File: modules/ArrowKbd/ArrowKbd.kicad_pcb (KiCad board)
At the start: 2 copper layers, 40.6 x 40.6 mm, 42 parts, among them J1 2, J10 11, J11 12, J12 13, J13 A0, J14 A1, J15 A2, J16 A3, J17 A4, J18 A5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

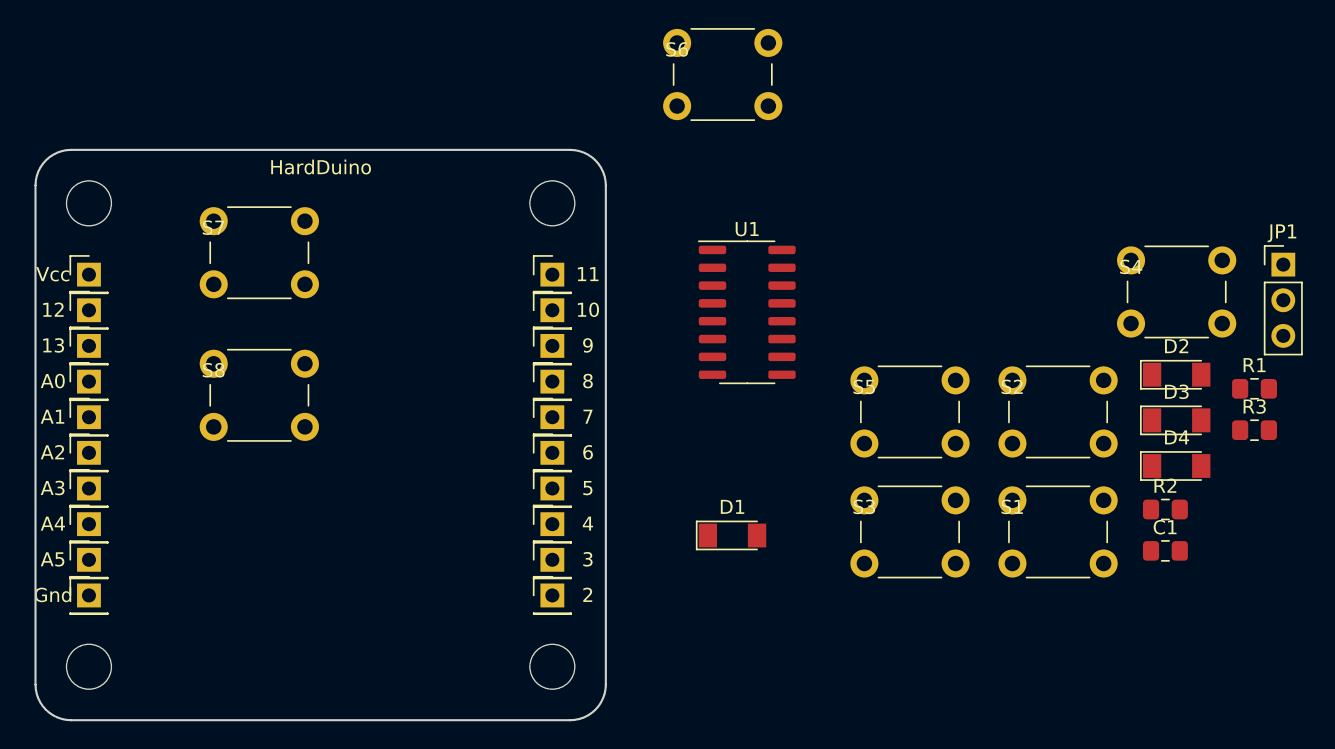
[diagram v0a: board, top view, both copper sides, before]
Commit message: Place Arrow Keys
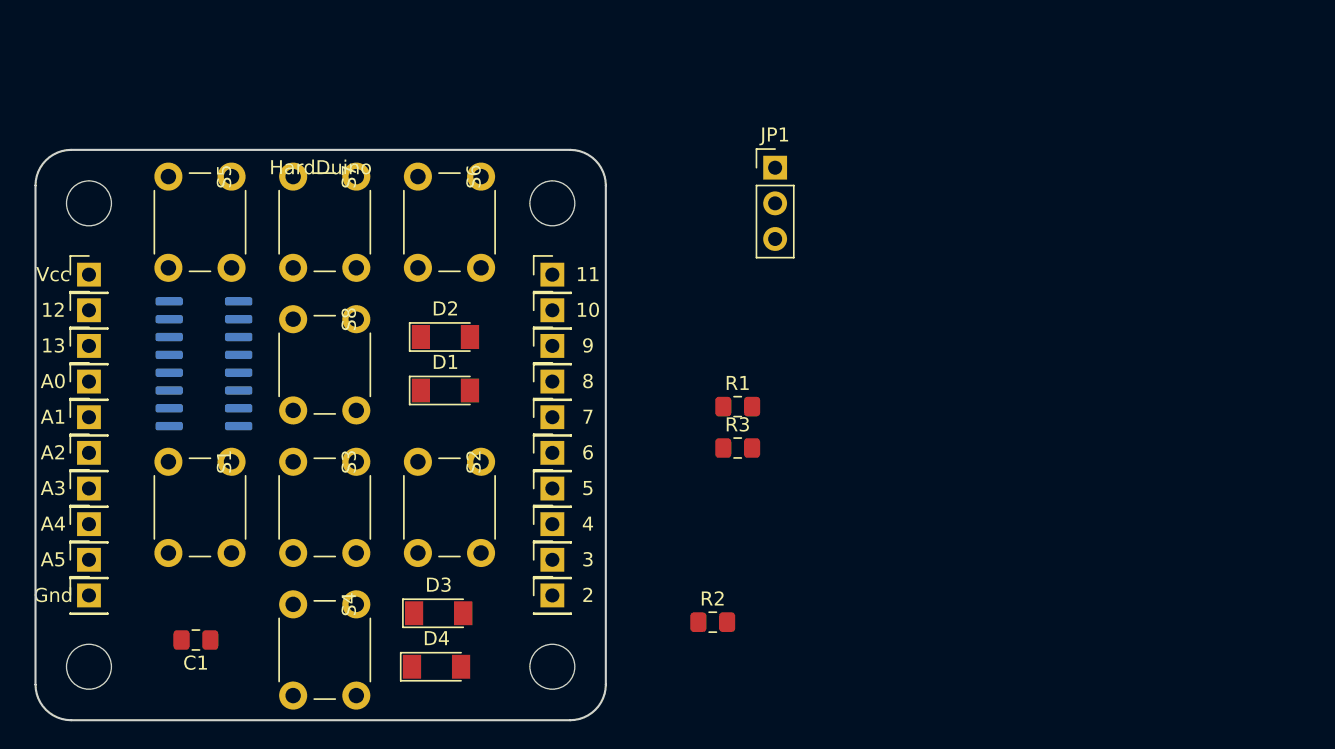
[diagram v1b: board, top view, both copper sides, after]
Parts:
- U1: moved to B.Cu
- moved C1 69.4 mm to (100.3, 85.7), turned to 180 degrees
- moved S4 60.4 mm to (111.8, 83.2), turned to 270 degrees
- moved S1 55.7 mm to (102.9, 73.0), turned to 270 degrees
- moved D4 54.6 mm to (117.5, 87.6)
- moved D3 54.4 mm to (117.6, 83.8)
- moved D2 52.2 mm to (118.1, 64.1)
- moved S5 47.4 mm to (102.9, 52.7), turned to 270 degrees
- moved U1 38.9 mm to (100.9, 66.0)
- moved S2 38.3 mm to (120.7, 73.0), turned to 270 degrees
- moved JP1 36.9 mm to (141.6, 52.1)
- moved R1 36.9 mm to (138.9, 69.1)
- moved R3 36.9 mm to (138.9, 72.0)
- moved S3 36.3 mm to (111.8, 73.0), turned to 270 degrees
- moved R2 33.2 mm to (137.2, 84.5)
- moved D1 22.9 mm to (118.1, 67.9)
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
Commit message: Arrow Kbd ready
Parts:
- C1, D1, D2, D3, D4: moved to B.Cu
- R1, R2: value R -> 10k
- R3: value R -> 10k; moved to B.Cu
- moved R2 46.1 mm to (97.2, 61.6), turned to 180 degrees
- moved R3 38.0 mm to (101.0, 71.8)
- moved R1 37.8 mm to (104.1, 83.8), turned to 270 degrees
- moved D4 25.4 mm to (117.2, 62.2)
- moved JP1 22.4 mm to (123.2, 64.8)
- moved D3 19.1 mm to (117.2, 64.8)
- moved C1 16.8 mm to (104.8, 69.5), turned to 90 degrees
- moved D2 4.55 mm to (117.2, 68.6)
- moved D1 3.31 mm to (117.2, 71.1)
- moved S8 1.27 mm to (111.8, 64.1)
- moved U1 1.25 mm to (99.7, 65.7)
- moved S1 0.63 mm to (102.9, 73.7)
- moved S2 0.63 mm to (120.7, 73.7)
- moved S3 0.63 mm to (111.8, 73.7)
- moved S5 0.32 mm to (102.9, 52.4)
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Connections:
- JP1 pad 1: Net-(JP1-Pad1) -> Net-(J8-Pad1)
- JP1 pad 3: Net-(JP1-Pad3) -> Net-(J7-Pad1)
- R1 pad 2: Net-(R1-Pad2) -> Net-(JP1-Pad2)
- R2 pad 1: Net-(R2-Pad1) -> Net-(J16-Pad1)
- R3 pad 1: VCC -> Net-(R3-Pad1)
- R3 pad 2: Net-(R3-Pad2) -> VCC
- S1 pad 2: Net-(R1-Pad2) -> Net-(JP1-Pad2)
- S2 pad 2: Net-(R1-Pad2) -> Net-(JP1-Pad2)
- S3 pad 2: Net-(R1-Pad2) -> Net-(JP1-Pad2)
- S4 pad 2: Net-(R1-Pad2) -> Net-(JP1-Pad2)
- S5 pad 2: Net-(R2-Pad1) -> Net-(J16-Pad1)
- S6 pad 2: Net-(R2-Pad1) -> Net-(J16-Pad1)
- S7 pad 2: Net-(R2-Pad1) -> Net-(J16-Pad1)
- S8 pad 2: Net-(R2-Pad1) -> Net-(J16-Pad1)
- U1 pad 1: GND -> Net-(R3-Pad1)
- U1 pad 10: Net-(U1-Pad10) -> Net-(D3-Pad1)
- U1 pad 11: Net-(U1-Pad11) -> Net-(D2-Pad1)
- U1 pad 12: Net-(U1-Pad12) -> Net-(D1-Pad1)
- U1 pad 13: Net-(R3-Pad2) -> Net-(J11-Pad1)
- U1 pad 14: Net-(R3-Pad2) -> Net-(J12-Pad1)
- U1 pad 15: Net-(R3-Pad2) -> GND
- U1 pad 4: Net-(D1-Pad1) -> Net-(U1-Pad4)
- U1 pad 5: Net-(D2-Pad1) -> Net-(U1-Pad5)
- U1 pad 6: Net-(D3-Pad1) -> Net-(U1-Pad6)
- U1 pad 7: Net-(D4-Pad1) -> Net-(U1-Pad7)
- U1 pad 9: Net-(U1-Pad9) -> Net-(D4-Pad1)
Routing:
- net Net-(JP1-Pad2): track 0.00 -> 55.9 mm
- net Net-(J16-Pad1): track 0.00 -> 48.4 mm
- net VCC: track 0.00 -> 47.4 mm, vias 0 -> 1
- net Net-(D1-Pad2): track 0.00 -> 37.9 mm
- net Net-(D3-Pad2): track 0.00 -> 36.9 mm
- net GND: track 0.00 -> 36.8 mm, vias 0 -> 2
- net Net-(D4-Pad2): track 0.00 -> 27.6 mm
- net Net-(D2-Pad2): track 0.00 -> 18.1 mm
- net Net-(D1-Pad1): track 0.00 -> 16.5 mm
- net Net-(D2-Pad1): track 0.00 -> 15.6 mm
- net Net-(D3-Pad1): track 0.00 -> 15.1 mm
- net Net-(J11-Pad1): track 0.00 -> 14.6 mm
- net Net-(D4-Pad1): track 0.00 -> 13.6 mm
- net Net-(J12-Pad1): track 0.00 -> 13.4 mm
- net Net-(R3-Pad1): track 0.00 -> 4.00 mm
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
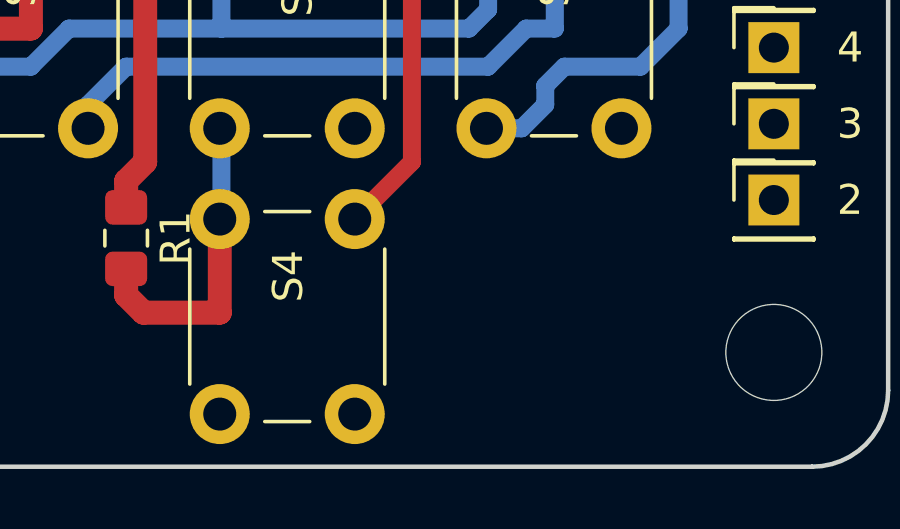
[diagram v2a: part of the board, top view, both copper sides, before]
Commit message: Add date. Add polygon.
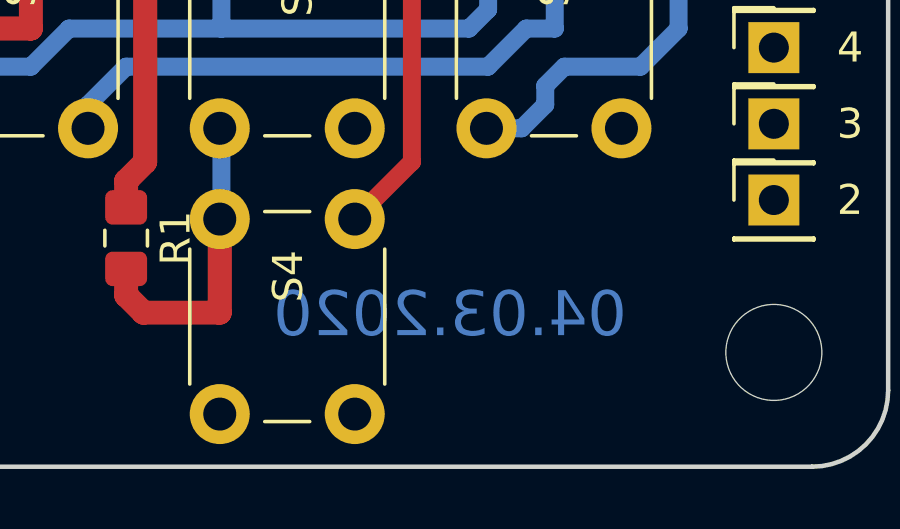
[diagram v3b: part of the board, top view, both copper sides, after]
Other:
- board text added: "04.03.2020"
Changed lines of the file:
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@@
   (general
     (thickness 1.6)
-    (drawings 29)
+    (drawings 30)
     (tracks 167)
     (zones 0)
@@
   )
   (setup
-    (last_trace_width 0.6)
+    (last_trace_width 0.25)
     (user_trace_width 0.4)
     (user_trace_width 0.5)
@@
     )
   )
+  (gr_text 04.03.2020 (at 114.935 86.36) (layer B.Cu)
+    (effects (font (size 1.5 1.5) (thickness 0.3)) (justify mirror))
+  )
   (gr_text HardDuino (at 109.5375 61.595) (layer F.SilkS)
     (effects (font (size 1 1) (thickness 0.15)))
@@
   (gr_line (start 129.54 53.34) (end 129.54 88.9) (layer Edge.Cuts) (width 0.15))
   (gr_line (start 91.44 50.8) (end 127 50.8) (layer Edge.Cuts) (width 0.15))
-  (via (at 99.695 63.8175) (size 1.6) (drill 0.9) (layers F.Cu B.Cu) (net 20))
-  (via (at 100.0125 69.5325) (size 1.6) (drill 0.9) (layers F.Cu B.Cu) (net 20))
   (segment (start 123.19 69.85) (end 125.73 67.31) (width 0.6) (layer B.Cu) (net 7))
   (segment (start 123.19 64.77) (end 125.73 64.77) (width 0.6) (layer B.Cu) (net 8))
@@
   (segment (start 102.17 70.1675) (end 103.5775 70.1675) (width 0.6) (layer B.Cu) (net 19))
   (segment (start 103.5775 70.1675) (end 103.895 70.485) (width 0.6) (layer B.Cu) (net 19))
+  (via (at 99.695 63.8175) (size 1.6) (drill 0.9) (layers F.Cu B.Cu) (net 20))
+  (via (at 100.0125 69.5325) (size 1.6) (drill 0.9) (layers F.Cu B.Cu) (net 20))
   (segment (start 102.17 68.8975) (end 103.505 68.8975) (width 0.6) (layer B.Cu) (net 20))
   (segment (start 103.505 68.8975) (end 103.895 68.5075) (width 0.6) (layer B.Cu) (net 20))

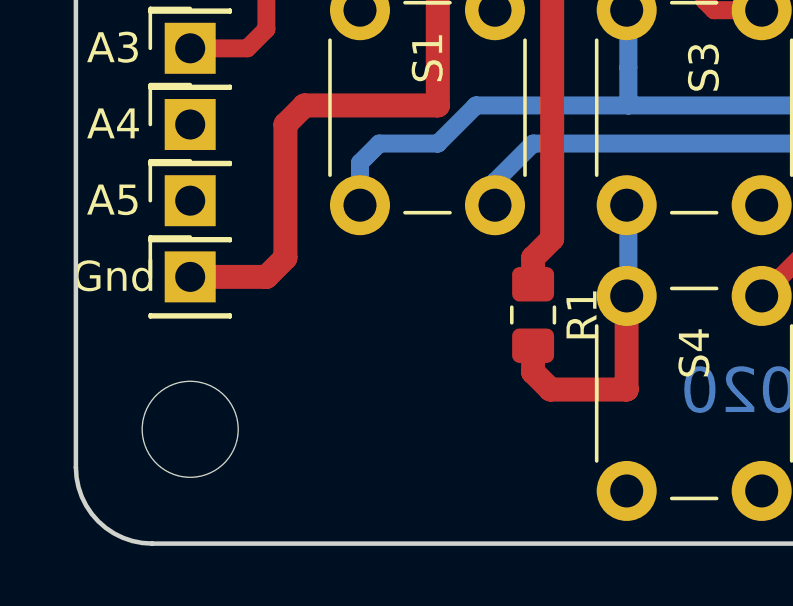
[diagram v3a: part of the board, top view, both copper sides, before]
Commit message: Add gnd symbol
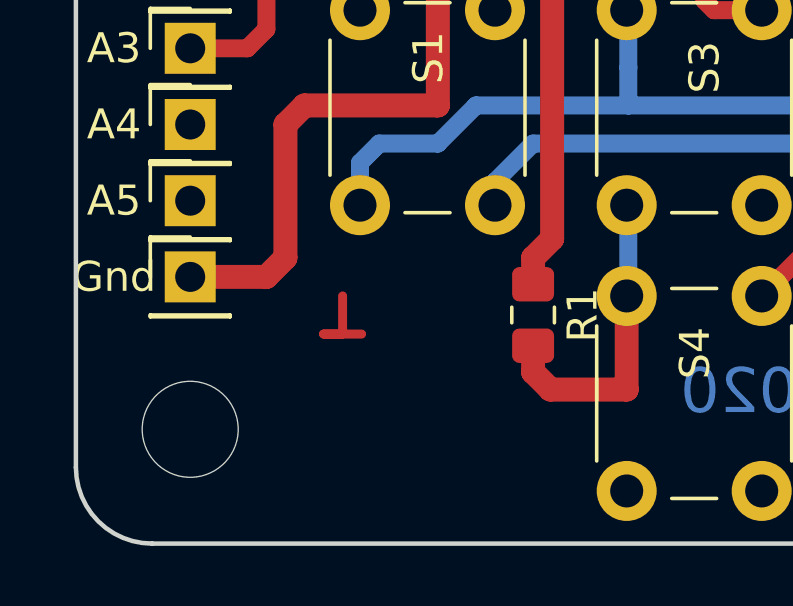
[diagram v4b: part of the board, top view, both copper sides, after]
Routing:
- net (no net): track 0.00 -> 3.17 mm
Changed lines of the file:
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@@
     (thickness 1.6)
     (drawings 30)
-    (tracks 167)
+    (tracks 170)
     (zones 0)
     (modules 42)
@@
   (gr_line (start 129.54 53.34) (end 129.54 88.9) (layer Edge.Cuts) (width 0.15))
   (gr_line (start 91.44 50.8) (end 127 50.8) (layer Edge.Cuts) (width 0.15))
+  (segment (start 97.79 83.185) (end 97.79 84.455) (width 0.3) (layer F.Cu) (net 0))
+  (segment (start 97.79 84.455) (end 97.155 84.455) (width 0.3) (layer F.Cu) (net 0))
+  (segment (start 97.155 84.455) (end 98.425 84.455) (width 0.3) (layer F.Cu) (net 0))
   (segment (start 123.19 69.85) (end 125.73 67.31) (width 0.6) (layer B.Cu) (net 7))
   (segment (start 123.19 64.77) (end 125.73 64.77) (width 0.6) (layer B.Cu) (net 8))
